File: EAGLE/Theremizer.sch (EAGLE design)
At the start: 93 parts, among them J1 3x2 M, J2 1x6 M, J4 POWER_JACK, Q1 PMV45EN2R, Q2 J310, Q3 J310, Q4 2N5088, Q5 2N5088, Q6 2N5088, Q7 2N5088, SW1 !RESET, U1 NCP1117ST50T3G, U2 MCU-ATMEGA328P-AU(TQFP32), X1 16 MHz

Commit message: Inital board & bunch of schematic changes
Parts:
- removed Q5: 2N5088, transistor-npn:2N5088
- removed R20: 100K, rcl:R-US_R0402
- added ANTENNA: Antenna, wirepad:2,54/1,1
- added C28: 10n, rcl:C-EUC0402
- added C29, C32: 10u, rcl:C-EUC0402
- added C30: 2.2n, rcl:C-EUC0402
- added C31: 100u, rcl:C-EUC0402
- added C33, C34: (no value), rcl:C-TRIMM808
- added C35: .1u, rcl:C-EUC0805K
- added IC2: NE5532D, linear:NE5532D
- added IC3: TL072D, linear:TL072D
- added J3, J5: AUDIO_JACK_TRS_0.25"_PTH_RA, SparkFun-Connectors:AUDIO_JACK_TRS_0.25"_PTH_RA
- added L4: 100u, rcl:L-US6000-XXX-RC
- added R34, R35: 10k, pot:TRIM_US-PT10
- added R36, R37, R45, R47: 100k, pot:TRIM_US-ECP10P
- added R38, R39: 470, rcl:R-US_R0402
- added R40, R41, R42: 10k, rcl:R-US_R0402
- added R43, R44: 10k, pot:TRIM_US-ECP10P
- added R46, R48: 50K, rcl:R-US_R0402
- added U4: LTC2645CMS-L8PBF, LTC2645CMS-L8PBF:LTC2645CMS-L8PBF
- C11: value (none) -> 100u
- C15: value 10uF -> 10u
- C16: value 2.2nF -> 2.2n
- C17: value 470pF -> 470p
- C21: value 220nF -> 300pF
- C22: value (none) -> .1u; device rcl:C-EUC0402 -> rcl:C-EUC0805K; DESC (none) -> CAP CER 30PF 50V C0G/NP0 0805; MFR (none) -> Samsung; MPN (none) -> CL21C300JBANNNC
- C27: value (none) -> 10n
- L1: value 1mH -> 1m
- L2: value 1mH -> 10mH
- L3: value (none) -> 1m
- Q4: value 2N5088 -> J310; device transistor-npn:2N5088 -> transistor-small-signal:J310
- R25, R30: value 470 -> 100
- R26: value 2.2K -> 10k; device rcl:R-US_R0402 -> pot:TRIM_US-PT10
- R27: value 470 -> 10k; device rcl:R-US_R0402 -> pot:TRIM_US-PT10
- R29: value (none) -> 100
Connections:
- removed net SIGNAL_INPUT: C27.1, MX1.IF, R7.1
- new net ADC6: R43.S, U2.ADC6
- new net ADC7: R44.S, U2.ADC7
- new net AUDIO_INPUT: C11.1, J5.RING-NORM
- new net N$39: C11.2, R26.E
- new net N$40: IC2A.-IN, R26.A, R36.E
- new net N$41: C29.1, IC2A.OUT, R36.A, R36.S
- new net N$42: C29.2, R39.2
- new net N$43: C28.2, R38.2
- new net N$44: Q4.G, R38.1, R39.1
- new net N$45: C30.1, C32.2, L4.2, Q4.D
- new net N$46: C31.2, Q4.S, R40.1
- new net N$47: C32.1, R35.E
- new net N$48: IC2B.-IN, R35.A, R37.E
- new net N$49: IC2B.OUT, R28.2, R37.A, R37.S
- new net N$50: IC3A.OUT, R45.A, R45.S, R7.1
- new net N$52: IC3B.-IN, R47.E, R48.2
- new net N$53: IC3B.OUT, J3.RING-NORM, R47.A, R47.S
- new net PWM_A: U2.PD5(T1), U4.INA
- new net PWM_B: U2.PD6(AIN0), U4.INB
- new net THEREMIN_OUT: C27.1, MX1.IF, R46.1
- net +15V: now also C30.2, IC2P.V+, IC3P.V+, L4.1, R25.2, R41.1; no longer Q4.C, Q5.C
- net +5V: now also C22.1, C35.1, R43.E, R44.E, U4.*PD, U4.IDLSEL, U4.IOVCC, U4.VCC
- net -15V: now also IC2P.V-, IC3P.V-
- net ANTENNA: now also ANTENNA.P
- net FILTER_OUTPUT: now also R48.1
- net FREQ_CV: now also IC1.12, R21.1, U4.VOUTA; no longer R20.1
- net GND: now also C31.1, C33.A, C34.A, C35.2, IC3A.+IN, IC3B.+IN, J3.EARTH-NORM, J3.TIP-NORM, J5.EARTH-NORM, J5.TIP-NORM, R27.A, R27.S, R30.1, R34.A, R40.2, R42.1, R43.A, R44.A, U4.GND, U4.GND_2, U4.REFSEL; no longer C11.2, R25.1, R26.1, R27.1, R30.2
- net N$19: now also IC3A.-IN, R45.E, R46.2; no longer IC1.12, R20.2, R21.1
- net N$26: now also C33.E; no longer C22.1
- net N$28: now also IC2A.+IN, R25.1, R30.2; no longer Q4.E, Q5.B, R26.2
- net N$29: now also IC2B.+IN, R41.2, R42.2; no longer Q5.E, R27.2, R28.2
- net N$32: now also C34.E; no longer C11.1
- net N$34: now also R34.E; no longer R25.2
- net N$35: now also C28.1; no longer Q4.B
- net N$38: now also R27.E; no longer R30.1
- net RES_CV: now also U4.VOUTB
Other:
- note added: "Filter Cutoff and Resonance Control"
- moved on the sheet: C11, C15, C16, C17, C18, C21, C27, C6, L1, L2, MX1, Q2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

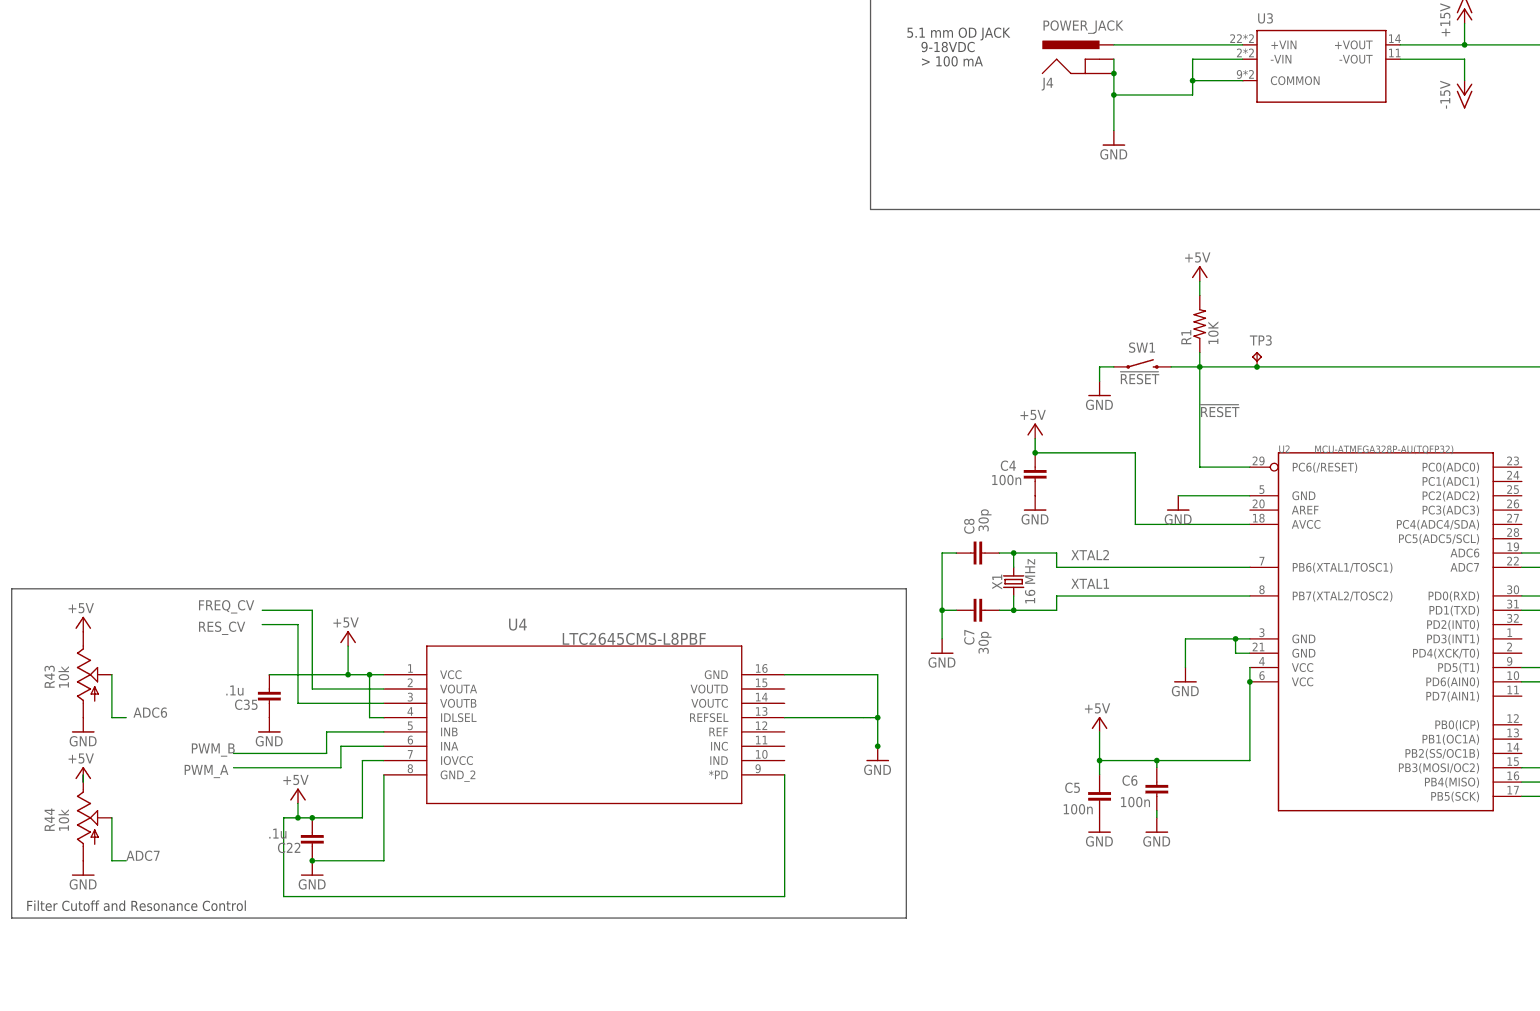
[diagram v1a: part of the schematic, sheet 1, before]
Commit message: Package size change
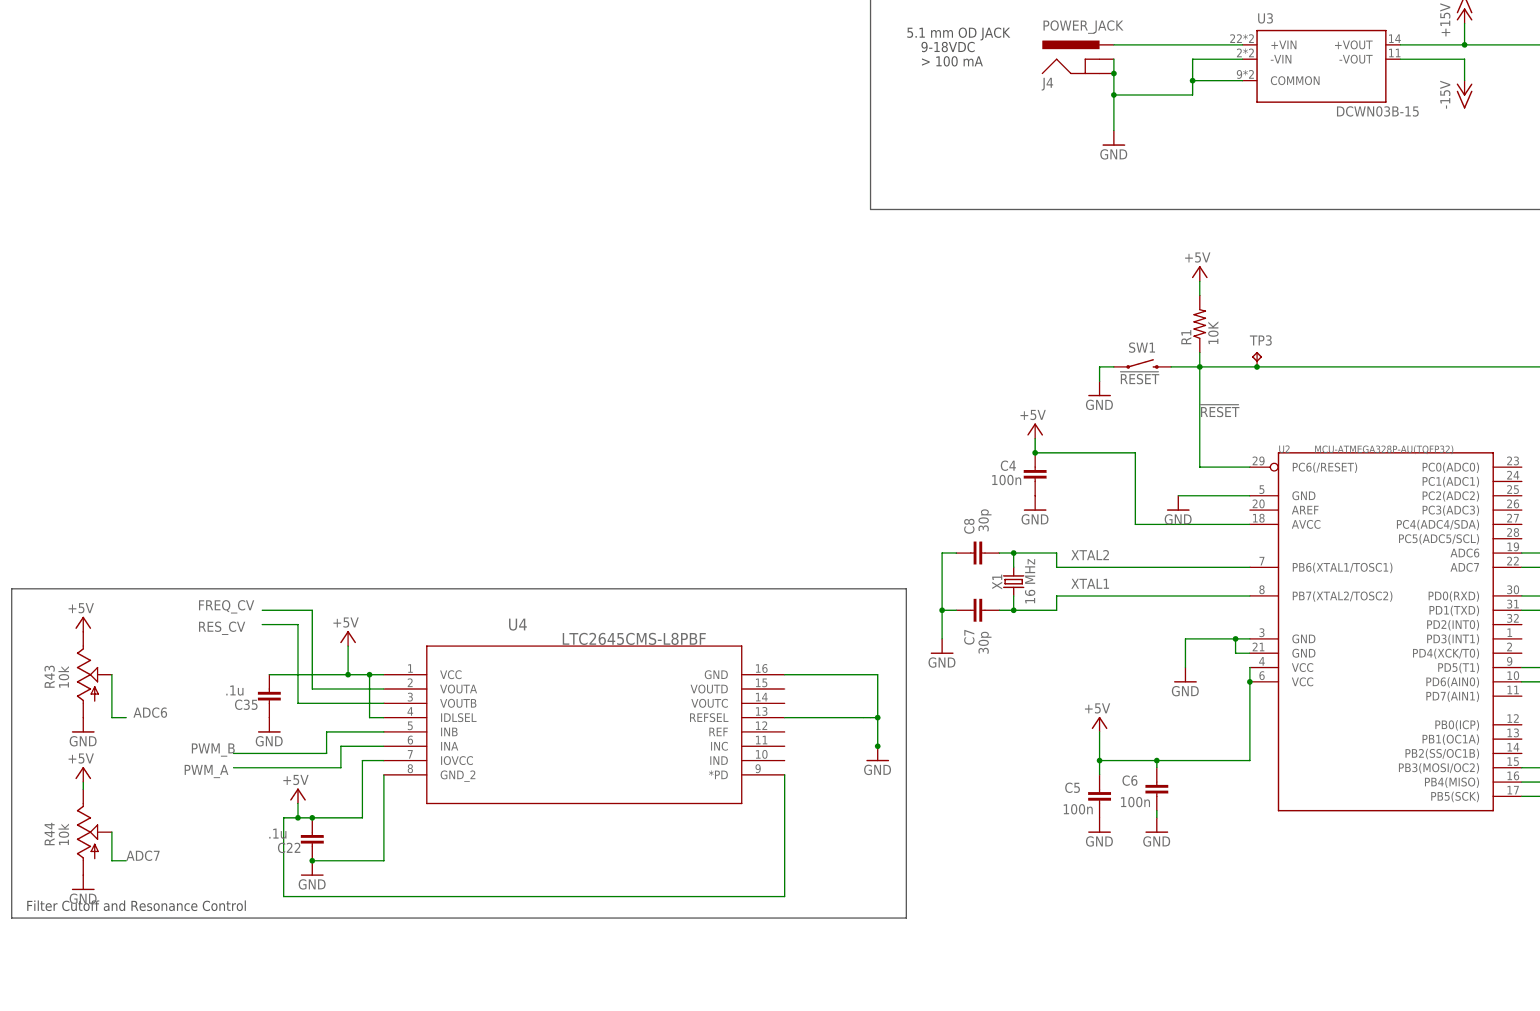
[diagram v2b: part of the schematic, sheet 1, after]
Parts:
- C10, C12, C9: device rcl:C-EUC0402 -> rcl:C-EUC0805
- C18: value 100nF -> 100n
- C25: value (none) -> 100n
- IC1: value (none) -> AS3320
- R10, R12, R13, R14, R15, R16, R17, R18, R19, R21, R22, R23, R46, R48, R7, R9: device rcl:R-US_R0402 -> rcl:R-US_R0805
- U3: value (none) -> DCWN03B-15
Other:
- moved on the sheet: R44

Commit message: Almost complete BOM
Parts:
- C11, C13, C15, C16, C17, C18, C19, C20, C21, C23, C24, C25, C26, C27, C28, C29, C30, C31, C32: device rcl:C-EUC0402 -> rcl:C-EUC0805
- C14: device rcl:C-USC0402 -> rcl:C-EUC0805
- R24, R25, R28, R29, R30, R31, R32, R33, R38, R39, R40, R41, R42: device rcl:R-US_R0402 -> rcl:R-US_R0805

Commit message: Test point for filter out
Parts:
- added FILTER_OUT: TPB2,54, testpad:TPB2,54
- C1, C2, C3, C35, C4, C5, C6, C7, C8: device rcl:C-EUC0805K -> rcl:C-EUC0805
- C10, C12, C13, C21, C9: value 300pF -> 300p
- C20: value 100nF -> 100n
- C33, C34: value (none) -> 8-100p
- L2: value 10mH -> 10m
- R11: device rcl:R-US_R0402 -> rcl:R-US_R0805
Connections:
- net FILTER_OUTPUT: now also FILTER_OUT.TP
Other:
- note added: "DAC"

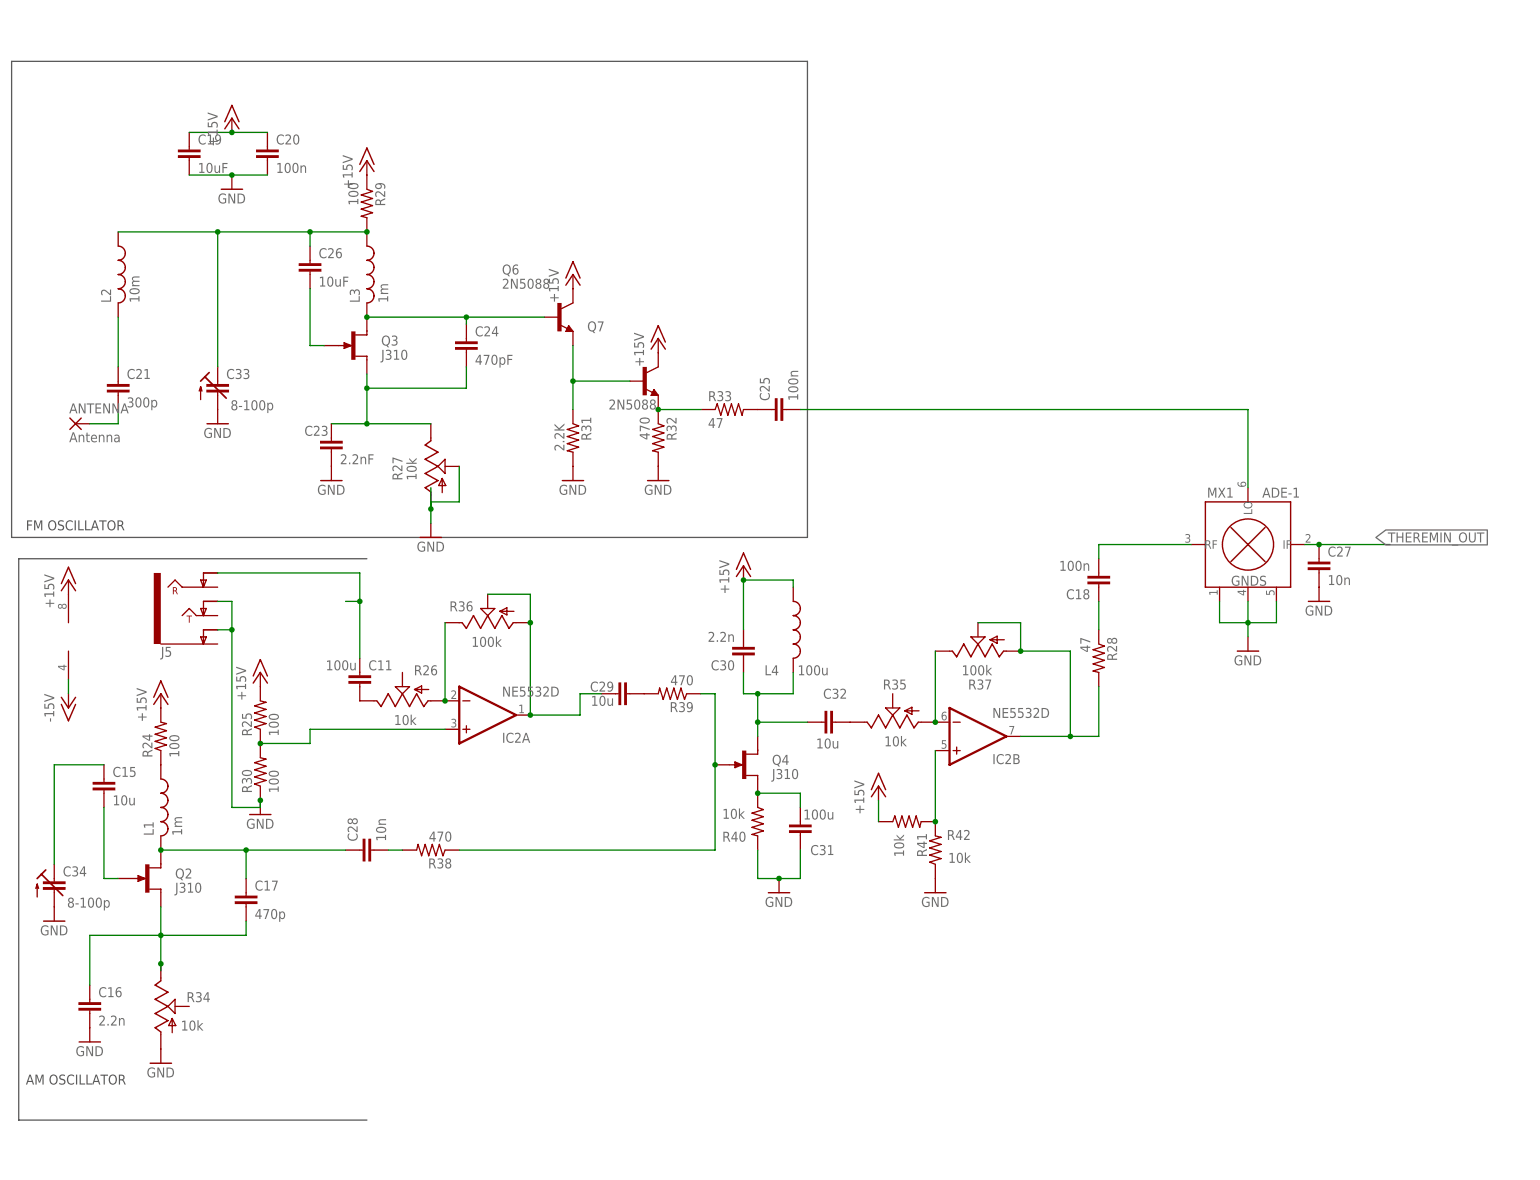
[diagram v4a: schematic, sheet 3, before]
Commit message: Added bypass, new mixer
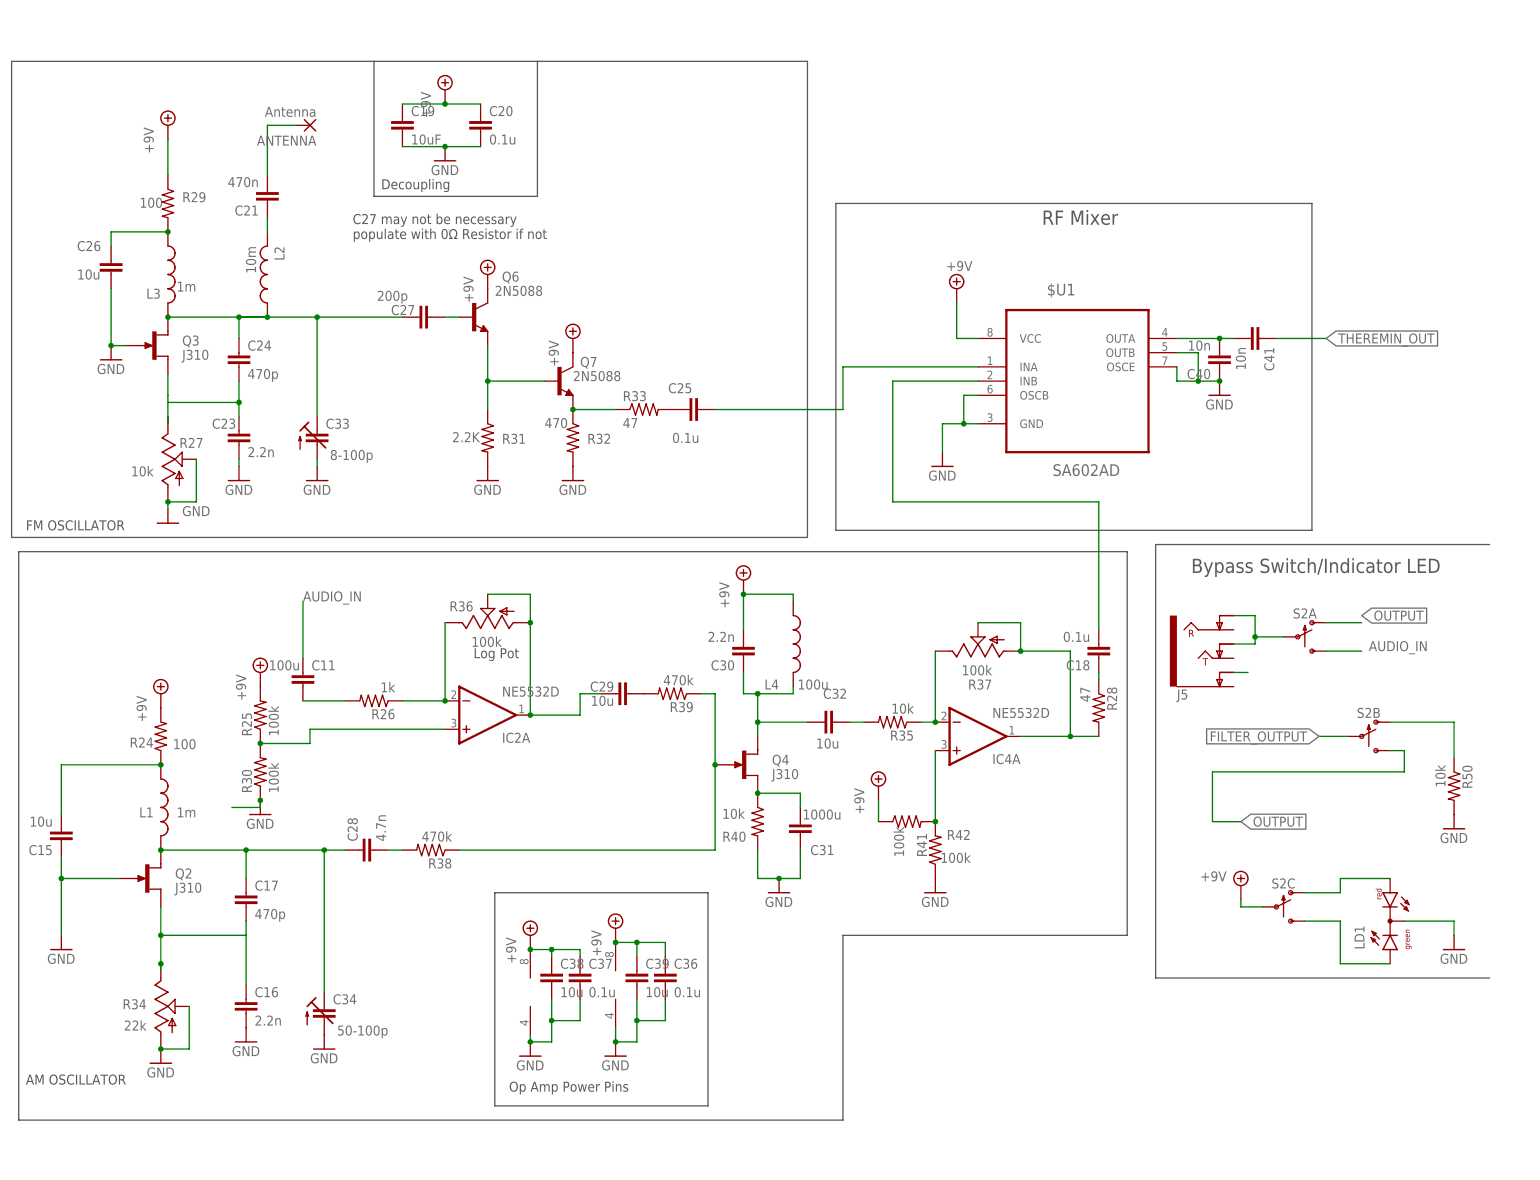
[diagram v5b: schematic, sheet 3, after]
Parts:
- removed MX1: ADE-1, minickts (1):ADE-1
- added $U1: SA602AD, SA602AN:SA602AD
- added C36, C37: 0.1u, rcl:C-EUC0805
- added C38, C39: 10u, rcl:C-EUC0805
- added C40, C41: 10n, rcl:C-EUC0805
- added D4: M7, diode:DIODE-SMB
- added IC4: NE5532D, linear:NE5532D
- added LD1: (no value), led:DUOLED-RG-C
- added R20, R49: 0, rcl:R-US_R0805
- added R50: 10k, rcl:R-US_R0805
- added S2: SWITCH-3PDT-PTH-STOMP, SparkFun-Switches:SWITCH-3PDT-PTH-STOMP
- C18, C20, C25: value 100n -> 0.1u
- C21: value 300p -> 470n
- C23: value 2.2nF -> 2.2n
- C24: value 470pF -> 470p
- C26: value 10uF -> 10u
- C27: value 10n -> 200p
- C28: value 10n -> 4.7n
- C31: value 100u -> 1000u
- C34: value 8-100p -> 50-100p
- R25, R30: value 100 -> 100k
- R26: value 10k -> 1k; device pot:TRIM_US-PT10 -> rcl:R-US_R0805
- R34: value 10k -> 22k
- R35: device pot:TRIM_US-PT10 -> rcl:R-US_R0805
- R38, R39: value 470 -> 470k
- R41, R42: value 10k -> 100k
- R8: value DNP or 0 -> 0
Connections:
- removed net 9V: J4.PWR, U3.+VIN
- removed net AUDIO_INPUT: C11.1, J5.RING-NORM
- removed net N$32 (its old number): C15.1, C34.E
- new net +9V: $U1.VCC, S2C.P
- new net AUDIO_IN: C11.1, S2A.S
- new net N$38: R50.1, S2B.O
- new net N$51: D1.A, D4.A, J4.PWR
- new net N$54: D4.C, U3.+VIN
- new net N$55: R20.1, U3.+VOUT
- new net N$56: R49.1, U3.-VOUT
- new net N$57: C26.1, L3.1, R29.2
- new net N$58: LD1.AG, S2C.S
- new net OUTPUT: IC3B.OUT, J3.RING-NORM, J3.TIP-NORM, R47.A, R47.S, S2A.O, S2B.S
- net +15V: now also C36.1, C37.1, C38.1, C39.1, IC4P.V+, R20.2; no longer D1.A, U3.+VOUT
- net -15V: now also R49.2; no longer IC2P.V-, U3.-VOUT
- net FILTER_OUTPUT: now also S2B.P
- net GND: now also $U1.GND, $U1.OSCB, $U1.OSCE, $U1.OUTB, C15.1, C26.2, C36.2, C37.2, C38.2, C39.2, C40.1, IC2P.V-, IC4P.V-, LD1.C, Q2.G, Q3.G, R34.S, R50.2; no longer C27.2, J3.TIP-NORM, J5.EARTH-NORM, J5.TIP-NORM, MX1.GND@1, MX1.GND@2, MX1.GND@3
- net N$22: now also C15.2
- net N$24: now also $U1.INA; no longer MX1.LO
- net N$26: now also C24.1, C27.1, L3.2, Q3.D; no longer C26.1, L3.1, R29.2
- net N$27: now also C27.2; no longer C24.1, L3.2, Q3.D
- net N$29: now also IC4A.+IN; no longer IC2B.+IN
- net N$33: now also C32.1, R35.2; no longer C15.2, Q2.G
- net N$35: now also C34.E
- net N$36: now also $U1.INB; no longer MX1.RF
- net N$37: now also J5.RING-NORM, J5.TIP-NORM, S2A.P; no longer C26.2, Q3.G
- net N$39: now also R26.2; no longer R26.E
- net N$40: now also R26.1; no longer R26.A
- net N$47: now also J5.EARTH-NORM; no longer C32.1, R35.E
- net N$48: now also IC4A.-IN, R35.1; no longer IC2B.-IN, R35.A
- net N$49: now also IC4A.OUT; no longer IC2B.OUT
- net N$53: now also LD1.AR, S2C.O; no longer IC3B.OUT, J3.RING-NORM, R47.A, R47.S
- net THEREMIN_OUT: now also $U1.OUTA, C40.2, C41.1, C41.2; no longer C27.1, MX1.IF
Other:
- note added: "Bypass Switch/Indicator LED"
- note added: "C27 may not be necessary populate with 0Ω Resistor if not"
- note added: "Decoupling"
- note added: "Log Pot"
- note added: "Op Amp Power Pins"
- note added: "PWM to Filter Cutoff and Resonance Control Voltage"
- note added: "Power for TL072"
- note added: "RF Mixer"
- note removed: "Filter Cutoff and Resonance Control"
- moved on the sheet: ANTENNA, C11, C15, C16, C18, C19, C20, C21, C23, C24, C25, C26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
